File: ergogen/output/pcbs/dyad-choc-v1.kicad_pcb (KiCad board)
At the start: 2 copper layers, 244.9 x 109.6 mm, 78 parts

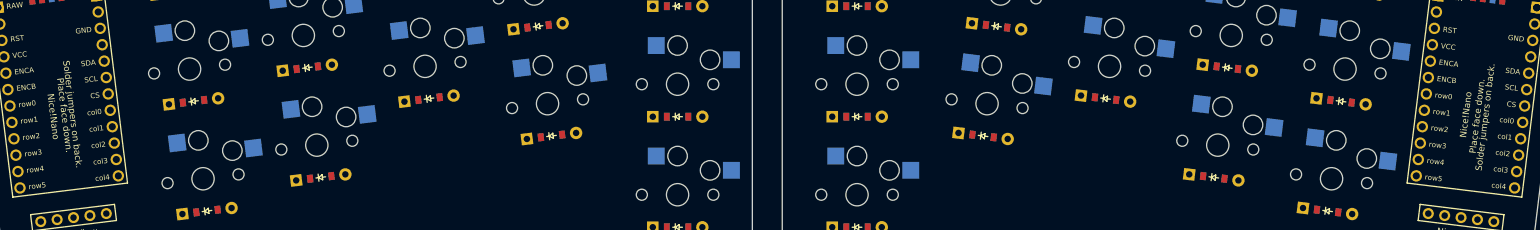
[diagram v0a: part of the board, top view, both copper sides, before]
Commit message: label reformating
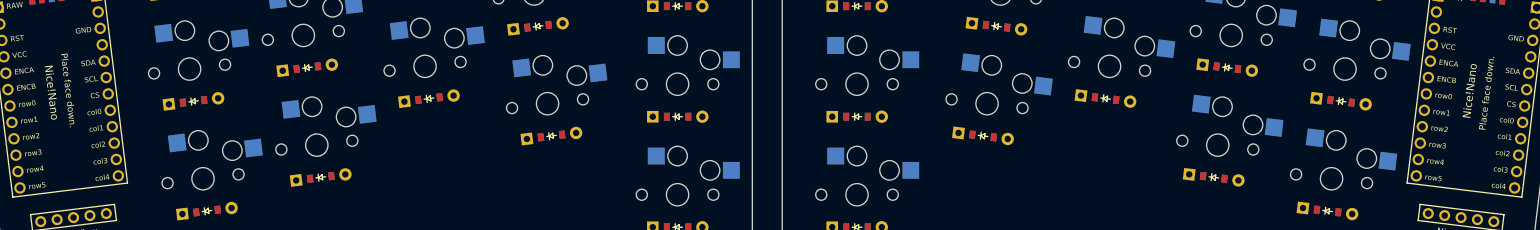
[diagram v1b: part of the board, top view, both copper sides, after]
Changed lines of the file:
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@@
   (page A3)
   (title_block
-    (title Dyad-V1)
+    (title dyad-choc-v1)
     (rev v1.0.0)
     (company Unknown)
@@
           (fp_text user col3 (at 11.43 -6.3 -7) (layer B.SilkS) (effects (font (size 0.8 0.8) (thickness 0.15)) (justify left mirror)))
           (fp_text user col4 (at 13.97 -6.3 -7) (layer B.SilkS) (effects (font (size 0.8 0.8) (thickness 0.15)) (justify left mirror)))
-          (fp_text user "Nice!Nano" (at 3.7 1.2 -97) (layer F.SilkS knockout) (effects (font (size 1.0 1.0) (thickness 0.15))))
-          (fp_text user "Place face down." (at 3.7 -0.55 -97) (layer F.SilkS) (effects (font (size 1.0 1.0) (thickness 0.15))))
-          (fp_text user "Solder jumpers on back." (at 3.7 -1.8 -97) (layer F.SilkS) (effects (font (size 1.0 1.0) (thickness 0.15))))
-          (fp_text user "Nice!Nano" (at 3.7 1.2 -97) (layer B.SilkS knockout) (effects (font (size 1.0 1.0) (thickness 0.15)) (justify mirror)))
-          (fp_text user "Place face down." (at 3.7 -0.55 -97) (layer B.SilkS) (effects (font (size 1.0 1.0) (thickness 0.15)) (justify mirror)))
-          (fp_text user "Solder jumpers on back." (at 3.7 -1.8 -97) (layer B.SilkS) (effects (font (size 1.0 1.0) (thickness 0.15)) (justify mirror)))
+          (fp_text user "Nice!Nano" (at 0 1 -97) (layer F.SilkS knockout) (effects (font (size 1.2 1.2) (thickness 0.30))))
+          (fp_text user "Place face down." (at 0 -1.6 -97) (layer F.SilkS) (effects (font (size 1.0 1.0) (thickness 0.15))))
           (pad 1 thru_hole circle (at -13.97 7.62 -97) (size 1.7526 1.7526) (drill 1.0922) (layers *.Cu *.SilkS *.Mask) (net 35 "RAW"))
           (pad 2 thru_hole circle (at -11.43 7.62 0) (size 1.7526 1.7526) (drill 1.0922) (layers *.Cu *.SilkS *.Mask) (net 36 "GND"))
@@
           (fp_text user col3 (at 11.43 -6.3 7) (layer B.SilkS) (effects (font (size 0.8 0.8) (thickness 0.15)) (justify left mirror)))
           (fp_text user col4 (at 13.97 -6.3 7) (layer B.SilkS) (effects (font (size 0.8 0.8) (thickness 0.15)) (justify left mirror)))
-          (fp_text user "Nice!Nano" (at 3.7 1.2 -83) (layer F.SilkS knockout) (effects (font (size 1.0 1.0) (thickness 0.15))))
-          (fp_text user "Place face down." (at 3.7 -0.55 -83) (layer F.SilkS) (effects (font (size 1.0 1.0) (thickness 0.15))))
-          (fp_text user "Solder jumpers on back." (at 3.7 -1.8 -83) (layer F.SilkS) (effects (font (size 1.0 1.0) (thickness 0.15))))
-          (fp_text user "Nice!Nano" (at 3.7 1.2 -83) (layer B.SilkS knockout) (effects (font (size 1.0 1.0) (thickness 0.15)) (justify mirror)))
-          (fp_text user "Place face down." (at 3.7 -0.55 -83) (layer B.SilkS) (effects (font (size 1.0 1.0) (thickness 0.15)) (justify mirror)))
-          (fp_text user "Solder jumpers on back." (at 3.7 -1.8 -83) (layer B.SilkS) (effects (font (size 1.0 1.0) (thickness 0.15)) (justify mirror)))
+          (fp_text user "Nice!Nano" (at 0 1 -83) (layer F.SilkS knockout) (effects (font (size 1.2 1.2) (thickness 0.30))))
+          (fp_text user "Place face down." (at 0 -1.6 -83) (layer F.SilkS) (effects (font (size 1.0 1.0) (thickness 0.15))))
           (pad 1 thru_hole circle (at -13.97 7.62 -83) (size 1.7526 1.7526) (drill 1.0922) (layers *.Cu *.SilkS *.Mask) (net 35 "RAW"))
           (pad 2 thru_hole circle (at -11.43 7.62 0) (size 1.7526 1.7526) (drill 1.0922) (layers *.Cu *.SilkS *.Mask) (net 36 "GND"))

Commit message: adding text labels
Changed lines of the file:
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@@
           (fp_text user col3 (at 11.43 -6.3 -7) (layer B.SilkS) (effects (font (size 0.8 0.8) (thickness 0.15)) (justify left mirror)))
           (fp_text user col4 (at 13.97 -6.3 -7) (layer B.SilkS) (effects (font (size 0.8 0.8) (thickness 0.15)) (justify left mirror)))
-          (fp_text user "Nice!Nano" (at 0 1 -97) (layer F.SilkS knockout) (effects (font (size 1.2 1.2) (thickness 0.30))))
+          (fp_text user "Nice!Nano" (at 0 1 -97) (layer F.SilkS knockout) (effects (font (size 1.2 1.2) (thickness 0.20))))
           (fp_text user "Place face down." (at 0 -1.6 -97) (layer F.SilkS) (effects (font (size 1.0 1.0) (thickness 0.15))))
           (pad 1 thru_hole circle (at -13.97 7.62 -97) (size 1.7526 1.7526) (drill 1.0922) (layers *.Cu *.SilkS *.Mask) (net 35 "RAW"))
@@
           (fp_text user col3 (at 11.43 -6.3 7) (layer B.SilkS) (effects (font (size 0.8 0.8) (thickness 0.15)) (justify left mirror)))
           (fp_text user col4 (at 13.97 -6.3 7) (layer B.SilkS) (effects (font (size 0.8 0.8) (thickness 0.15)) (justify left mirror)))
-          (fp_text user "Nice!Nano" (at 0 1 -83) (layer F.SilkS knockout) (effects (font (size 1.2 1.2) (thickness 0.30))))
+          (fp_text user "Nice!Nano" (at 0 1 -83) (layer F.SilkS knockout) (effects (font (size 1.2 1.2) (thickness 0.20))))
           (fp_text user "Place face down." (at 0 -1.6 -83) (layer F.SilkS) (effects (font (size 1.0 1.0) (thickness 0.15))))
           (pad 1 thru_hole circle (at -13.97 7.62 -83) (size 1.7526 1.7526) (drill 1.0922) (layers *.Cu *.SilkS *.Mask) (net 35 "RAW"))
@@
                 (pad 2 smd rect (at -0.75 2.075 -7) (size 0.9 1.25) (layers F.Cu F.Paste F.Mask) (net 35 "RAW"))
                 (pad 3 smd rect (at -2.25 2.075 -7) (size 0.9 1.25) (layers F.Cu F.Paste F.Mask))
+                (fp_text user "Power" (at 0 3.6 -7) (layer F.SilkS knockout) (effects (font (size 0.8 0.8) (thickness 0.15))))
                 (fp_line (start 1.95 -1.35) (end -1.95 -1.35) (layer B.SilkS) (width 0.15))
                 (fp_line (start 0 -1.35) (end -3.3 -1.35) (layer B.SilkS) (width 0.15))
@@
                 (pad 2 smd rect (at 0.75 2.075 -7) (size 0.9 1.25) (layers B.Cu B.Paste B.Mask) (net 35 "RAW"))
                 (pad 3 smd rect (at 2.25 2.075 -7) (size 0.9 1.25) (layers B.Cu B.Paste B.Mask))
+                (fp_text user "Power" (at 0 3.6 -7) (layer F.SilkS knockout) (effects (font (size 0.8 0.8) (thickness 0.15))))
                 )
             (module E73:SPDT_C128955 (layer F.Cu)
@@
                 (pad 2 smd rect (at -0.75 2.075 7) (size 0.9 1.25) (layers F.Cu F.Paste F.Mask) (net 35 "RAW"))
                 (pad 3 smd rect (at -2.25 2.075 7) (size 0.9 1.25) (layers F.Cu F.Paste F.Mask))
+                (fp_text user "Power" (at 0 3.6 7) (layer F.SilkS knockout) (effects (font (size 0.8 0.8) (thickness 0.15))))
                 (fp_line (start 1.95 -1.35) (end -1.95 -1.35) (layer B.SilkS) (width 0.15))
                 (fp_line (start 0 -1.35) (end -3.3 -1.35) (layer B.SilkS) (width 0.15))
@@
                 (pad 2 smd rect (at 0.75 2.075 7) (size 0.9 1.25) (layers B.Cu B.Paste B.Mask) (net 35 "RAW"))
                 (pad 3 smd rect (at 2.25 2.075 7) (size 0.9 1.25) (layers B.Cu B.Paste B.Mask))
+                (fp_text user "Power" (at 0 3.6 7) (layer F.SilkS knockout) (effects (font (size 0.8 0.8) (thickness 0.15))))
                 )
             (module lib:niceview_headers (layer F.Cu)
@@
       (pad "1" thru_hole circle (at -3.2 0 173) (size 2 2) (drill 1) (layers "*.Cu" "*.Mask") (net 36 "GND"))
       (pad "2" thru_hole circle (at 3.2 0 173) (size 2 2) (drill 1) (layers "*.Cu" "*.Mask") (net 37 "RST"))
+      (fp_text user "Reset" (at 0 -3 173) (layer F.SilkS knockout) (effects (font (size 0.8 0.8) (thickness 0.15))))
     )
     (module PTS636_SP43_LFS (layer F.Cu)
@@
       (pad "1" thru_hole circle (at -3.2 0 -173) (size 2 2) (drill 1) (layers "*.Cu" "*.Mask") (net 36 "GND"))
       (pad "2" thru_hole circle (at 3.2 0 -173) (size 2 2) (drill 1) (layers "*.Cu" "*.Mask") (net 37 "RST"))
+      (fp_text user "Reset" (at 0 -3 -173) (layer F.SilkS knockout) (effects (font (size 0.8 0.8) (thickness 0.15))))
     )
             (gr_line (start 220.5 171) (end 241.15492522211616 171) (angle 90) (layer Edge.Cuts) (width 0.15))

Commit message: iterating routes
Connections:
- net inner_default renamed inner_sole
- net mirror_inner_default renamed mirror_inner_sole
- net mirror_outer_default renamed mirror_outer_sole
- net mirror_pinkey_height_bottom renamed mirror_pinky_bottom
- net mirror_pinkey_height_home renamed mirror_pinky_home
- net mirror_pinkey_height_top renamed mirror_pinky_top
- net outer_default renamed outer_sole
- net pinkey_height_bottom renamed pinky_bottom
- net pinkey_height_home renamed pinky_home
- net pinkey_height_top renamed pinky_top
- D1 pad 1: (no net) -> P8
- D10 pad 1: (no net) -> P8
- D11 pad 1: (no net) -> P7
- D12 pad 1: (no net) -> P6
- D13 pad 1: (no net) -> P8
- D14 pad 1: (no net) -> P7
- D15 pad 1: (no net) -> P6
- D16 pad 1: (no net) -> P9
- D17 pad 1: (no net) -> P9
- D18 pad 1: (no net) -> P8
- D19 pad 1: (no net) -> P7
- D2 pad 1: (no net) -> P7
- D20 pad 1: (no net) -> P6
- D21 pad 1: (no net) -> P8
- D22 pad 1: (no net) -> P7
- D23 pad 1: (no net) -> P6
- D24 pad 1: (no net) -> P8
- D25 pad 1: (no net) -> P7
- D26 pad 1: (no net) -> P6
- D27 pad 1: (no net) -> P8
- D28 pad 1: (no net) -> P7
- D29 pad 1: (no net) -> P6
- D3 pad 1: (no net) -> P6
- D30 pad 1: (no net) -> P8
- D31 pad 1: (no net) -> P7
- D32 pad 1: (no net) -> P6
- D33 pad 1: (no net) -> P9
- D34 pad 1: (no net) -> P9
- D4 pad 1: (no net) -> P8
- D5 pad 1: (no net) -> P7
- D6 pad 1: (no net) -> P6
- D7 pad 1: (no net) -> P8
- D8 pad 1: (no net) -> P7
- D9 pad 1: (no net) -> P6
- MCU1 pad : P1 -> CS
- MCU1 pad 13: P1 -> CS
- MCU1 pad 17: P2 -> MOSI
- MCU1 pad 18: P3 -> SCK
- MCU2 pad : P1 -> CS
- MCU2 pad 13: P1 -> CS
- MCU2 pad 17: P2 -> MOSI
- MCU2 pad 18: P3 -> SCK
- Nice!View1 pad 1: NN_CS_SDA -> CS
- Nice!View1 pad 2: NN_VCC -> VCC
- Nice!View1 pad 3: NN_SCL_GND -> SCK
- Nice!View1 pad 4: NN_SDA_CS -> MOSI
- Nice!View2 pad 1: NN_CS_SDA -> CS
- Nice!View2 pad 2: NN_VCC -> VCC
- Nice!View2 pad 3: NN_SCL_GND -> SCK
- Nice!View2 pad 4: NN_SDA_CS -> MOSI
- S1 pad 1: (no net) -> P18
- S10 pad 1: (no net) -> P16
- S11 pad 1: (no net) -> P16
- S12 pad 1: (no net) -> P16
- S13 pad 1: (no net) -> P10
- S14 pad 1: (no net) -> P10
- S15 pad 1: (no net) -> P10
- S16 pad 1: (no net) -> P16
- S17 pad 1: (no net) -> P10
- S18 pad 1: (no net) -> P18
- S19 pad 1: (no net) -> P18
- S2 pad 1: (no net) -> P18
- S20 pad 1: (no net) -> P18
- S21 pad 1: (no net) -> P15
- S22 pad 1: (no net) -> P15
- S23 pad 1: (no net) -> P15
- S24 pad 1: (no net) -> P14
- S25 pad 1: (no net) -> P14
- S26 pad 1: (no net) -> P14
- S27 pad 1: (no net) -> P16
- S28 pad 1: (no net) -> P16
- S29 pad 1: (no net) -> P16
- S3 pad 1: (no net) -> P18
- S30 pad 1: (no net) -> P10
- S31 pad 1: (no net) -> P10
- S32 pad 1: (no net) -> P10
- S33 pad 1: (no net) -> P16
- S34 pad 1: (no net) -> P10
- S4 pad 1: (no net) -> P15
- S5 pad 1: (no net) -> P15
- S6 pad 1: (no net) -> P15
- S7 pad 1: (no net) -> P14
- S8 pad 1: (no net) -> P14
- S9 pad 1: (no net) -> P14

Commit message: completing routes
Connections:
- ? pad 1: RAW -> POSITIVE (x2)
- T1 pad 1: switch_from -> POSITIVE
- T2 pad 1: switch_from -> POSITIVE
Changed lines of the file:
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@@
 (net 55 "P4")
 (net 56 "P5")
-(net 57 "switch_from")
+(net 57 "POSITIVE")
   (net_class Default "This is the default net class."
     (clearance 0.2)
@@
 (add_net "P4")
 (add_net "P5")
-(add_net "switch_from")
+(add_net "POSITIVE")
   )
       (module PG1350 (layer F.Cu)
@@
         (fp_text user + (at 0 6.3 173) (layer B.SilkS) (effects (font (size 0.8 0.8) (thickness 0.15))))
         (fp_text user - (at 0 -6.3 173) (layer B.SilkS) (effects (font (size 0.8 0.8) (thickness 0.15))))
-        (pad 1 thru_hole rect (at 0 7.75 83) (size 1.4 1.4) (drill 0.8) (layers *.Cu *.SilkS *.Mask) (net 44 "RAW"))
+        (pad 1 thru_hole rect (at 0 7.75 83) (size 1.4 1.4) (drill 0.8) (layers *.Cu *.SilkS *.Mask) (net 57 "POSITIVE"))
         (pad 2 thru_hole circle (at 0 -7.75 83) (size 1.4 1.4) (drill 0.8) (layers *.Cu *.SilkS *.Mask) (net 45 "GND"))
         )
@@
         (fp_text user + (at 0 6.3 7) (layer B.SilkS) (effects (font (size 0.8 0.8) (thickness 0.15))))
         (fp_text user - (at 0 -6.3 7) (layer B.SilkS) (effects (font (size 0.8 0.8) (thickness 0.15))))
-        (pad 1 thru_hole rect (at 0 7.75 -83) (size 1.4 1.4) (drill 0.8) (layers *.Cu *.SilkS *.Mask) (net 44 "RAW"))
+        (pad 1 thru_hole rect (at 0 7.75 -83) (size 1.4 1.4) (drill 0.8) (layers *.Cu *.SilkS *.Mask) (net 57 "POSITIVE"))
         (pad 2 thru_hole circle (at 0 -7.75 -83) (size 1.4 1.4) (drill 0.8) (layers *.Cu *.SilkS *.Mask) (net 45 "GND"))
         )
@@
                 (pad "" smd rect (at -3.7 1.1 -7) (size 0.9 0.9) (layers B.Cu B.Paste B.Mask))
                 (pad "" smd rect (at -3.7 -1.1 -7) (size 0.9 0.9) (layers B.Cu B.Paste B.Mask))
-                (pad 1 smd rect (at -2.25 2.075 -7) (size 0.9 1.25) (layers B.Cu B.Paste B.Mask) (net 57 "switch_from"))
+                (pad 1 smd rect (at -2.25 2.075 -7) (size 0.9 1.25) (layers B.Cu B.Paste B.Mask) (net 57 "POSITIVE"))
                 (pad 2 smd rect (at 0.75 2.075 -7) (size 0.9 1.25) (layers B.Cu B.Paste B.Mask) (net 44 "RAW"))
                 (pad 3 smd rect (at 2.25 2.075 -7) (size 0.9 1.25) (layers B.Cu B.Paste B.Mask))
-                (fp_text user "Power" (at 0 3.6 -7) (layer F.SilkS knockout) (effects (font (size 0.8 0.8) (thickness 0.15))))
-                (fp_line (start 1.95 -1.35) (end -1.95 -1.35) (layer F.SilkS) (width 0.15))
-                (fp_line (start 0 -1.35) (end -3.3 -1.35) (layer F.SilkS) (width 0.15))
-                (fp_line (start -3.3 -1.35) (end -3.3 1.5) (layer F.SilkS) (width 0.15))
-                (fp_line (start -3.3 1.5) (end 3.3 1.5) (layer F.SilkS) (width 0.15))
-                (fp_line (start 3.3 1.5) (end 3.3 -1.35) (layer F.SilkS) (width 0.15))
-                (fp_line (start 0 -1.35) (end 3.3 -1.35) (layer F.SilkS) (width 0.15))
-                (pad "" smd rect (at 3.7 -1.1 -7) (size 0.9 0.9) (layers F.Cu F.Paste F.Mask))
-                (pad "" smd rect (at 3.7 1.1 -7) (size 0.9 0.9) (layers F.Cu F.Paste F.Mask))
-                (pad "" smd rect (at -3.7 1.1 -7) (size 0.9 0.9) (layers F.Cu F.Paste F.Mask))
-                (pad "" smd rect (at -3.7 -1.1 -7) (size 0.9 0.9) (layers F.Cu F.Paste F.Mask))
-                (pad 1 smd rect (at 2.25 2.075 -7) (size 0.9 1.25) (layers F.Cu F.Paste F.Mask) (net 57 "switch_from"))
-                (pad 2 smd rect (at -0.75 2.075 -7) (size 0.9 1.25) (layers F.Cu F.Paste F.Mask) (net 44 "RAW"))
-                (pad 3 smd rect (at -2.25 2.075 -7) (size 0.9 1.25) (layers F.Cu F.Paste F.Mask))
                 (fp_text user "Power" (at 0 3.6 -7) (layer F.SilkS knockout) (effects (font (size 0.8 0.8) (thickness 0.15))))
                 )
@@
                 (pad "" smd rect (at -3.7 1.1 7) (size 0.9 0.9) (layers B.Cu B.Paste B.Mask))
                 (pad "" smd rect (at -3.7 -1.1 7) (size 0.9 0.9) (layers B.Cu B.Paste B.Mask))
-                (pad 1 smd rect (at -2.25 2.075 7) (size 0.9 1.25) (layers B.Cu B.Paste B.Mask) (net 57 "switch_from"))
+                (pad 1 smd rect (at -2.25 2.075 7) (size 0.9 1.25) (layers B.Cu B.Paste B.Mask) (net 57 "POSITIVE"))
                 (pad 2 smd rect (at 0.75 2.075 7) (size 0.9 1.25) (layers B.Cu B.Paste B.Mask) (net 44 "RAW"))
                 (pad 3 smd rect (at 2.25 2.075 7) (size 0.9 1.25) (layers B.Cu B.Paste B.Mask))
                 (fp_text user "Power" (at 0 3.6 7) (layer F.SilkS knockout) (effects (font (size 0.8 0.8) (thickness 0.15))))
-                (fp_line (start 1.95 -1.35) (end -1.95 -1.35) (layer F.SilkS) (width 0.15))
-                (fp_line (start 0 -1.35) (end -3.3 -1.35) (layer F.SilkS) (width 0.15))
-                (fp_line (start -3.3 -1.35) (end -3.3 1.5) (layer F.SilkS) (width 0.15))
-                (fp_line (start -3.3 1.5) (end 3.3 1.5) (layer F.SilkS) (width 0.15))
-                (fp_line (start 3.3 1.5) (end 3.3 -1.35) (layer F.SilkS) (width 0.15))
-                (fp_line (start 0 -1.35) (end 3.3 -1.35) (layer F.SilkS) (width 0.15))
-                (pad "" smd rect (at 3.7 -1.1 7) (size 0.9 0.9) (layers F.Cu F.Paste F.Mask))
-                (pad "" smd rect (at 3.7 1.1 7) (size 0.9 0.9) (layers F.Cu F.Paste F.Mask))
-                (pad "" smd rect (at -3.7 1.1 7) (size 0.9 0.9) (layers F.Cu F.Paste F.Mask))
-                (pad "" smd rect (at -3.7 -1.1 7) (size 0.9 0.9) (layers F.Cu F.Paste F.Mask))
-                (pad 1 smd rect (at 2.25 2.075 7) (size 0.9 1.25) (layers F.Cu F.Paste F.Mask) (net 57 "switch_from"))
-                (pad 2 smd rect (at -0.75 2.075 7) (size 0.9 1.25) (layers F.Cu F.Paste F.Mask) (net 44 "RAW"))
-                (pad 3 smd rect (at -2.25 2.075 7) (size 0.9 1.25) (layers F.Cu F.Paste F.Mask))
-                (fp_text user "Power" (at 0 3.6 7) (layer F.SilkS knockout) (effects (font (size 0.8 0.8) (thickness 0.15))))
                 )

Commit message: continuing to refine
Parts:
- removed the ? at (321.7, 173.4)
- removed the ? at (110.7, 173.4)
- added ?: , Button_Switch_SMD:SW_SPST_B3U-1000P, F.Cu at (321.7, 173.4)
- added ?: , Button_Switch_SMD:SW_SPST_B3U-1000P, F.Cu at (114.3, 173.4)
- moved ? 3.60 mm to (108.7, 127.8), turned to 97 degrees
- moved D18 3.60 mm to (206.0, 165.0)
- moved D19 3.60 mm to (206.0, 148.0)
- moved D20 3.60 mm to (206.0, 131.0)
- moved D21 3.60 mm to (186.6, 151.0)
- moved D22 3.60 mm to (184.5, 134.1)
- moved D23 3.60 mm to (182.5, 117.2)
- moved D24 3.60 mm to (167.8, 145.2)
- moved D25 3.60 mm to (165.7, 128.3)
- moved D26 3.60 mm to (163.6, 111.5)
- moved D27 3.60 mm to (151.1, 157.3)
- moved D28 3.60 mm to (149.0, 140.5)
- moved D29 3.60 mm to (147.0, 123.6)
- moved D30 3.60 mm to (133.6, 162.5)
- moved D31 3.60 mm to (131.5, 145.6)
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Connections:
- T1 pad 1: POSITIVE -> RAW
- T1 pad 2: RAW -> POSITIVE
- T2 pad 1: POSITIVE -> RAW
- T2 pad 2: RAW -> POSTIVE
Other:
- board size 244.9 x 109.6 mm -> 238.4 x 105.9 mm

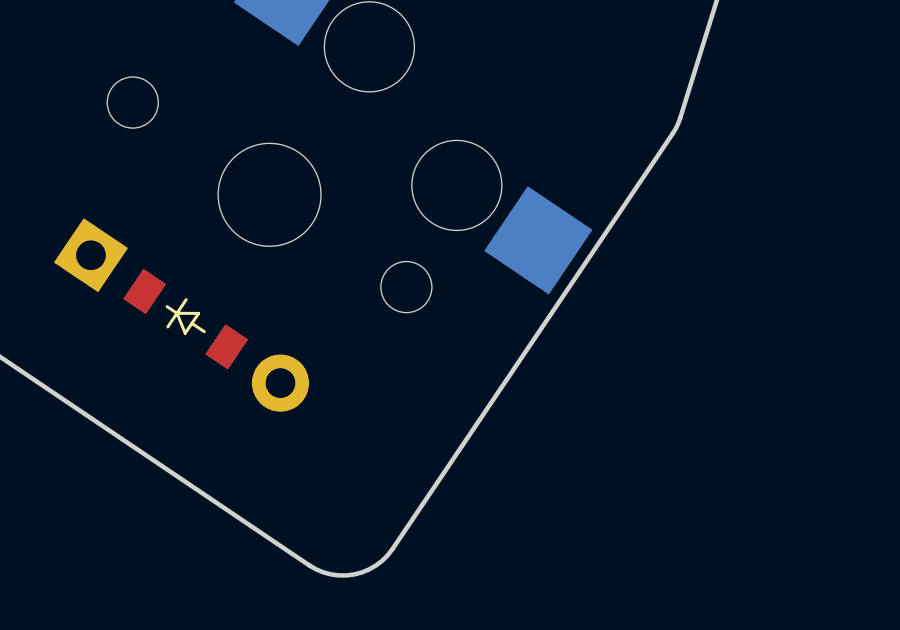
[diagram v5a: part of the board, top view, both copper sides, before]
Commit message: adding via example
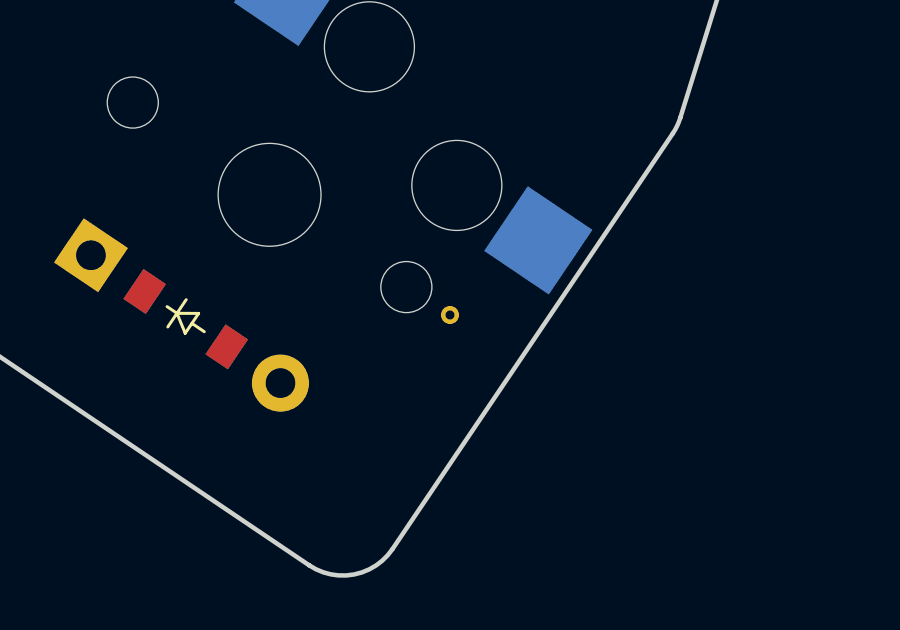
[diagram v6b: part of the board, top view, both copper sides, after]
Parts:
- added REF**: VIA-0.6mm, VIA-0.6mm, F.Cu at (319.3, 193.3)
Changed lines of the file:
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@@
 	  (pad 2 smd rect (at 1.7 0 187) (size 0.9 1.7) (layers F.Cu F.Paste F.Mask) (net 45 "GND"))
 		  )
+      (module VIA-0.6mm (layer F.Cu)
+      (at 319.2527186 193.29229289999998 -7)
+      (fp_text reference REF** (at 0 1.4) (layer F.SilkS) hide (effects (font (size 1 1) (thickness 0.15))))
+      (fp_text value VIA-0.6mm (at 0 -1.4) (layer F.Fab) hide (effects (font (size 1 1) (thickness 0.15))))
+      (pad 1 thru_hole circle (at 0 0) (size 0.6 0.6) (drill 0.3) (layers *.Cu) (zone_connect 2) (net 44 "RAW"))
+      )
             (gr_line (start 222 169.5) (end 239.6672239474708 169.5) (angle 90) (layer Edge.Cuts) (width 0.15))
 (gr_line (start 220 167.5) (end 220 118.5) (angle 90) (layer Edge.Cuts) (width 0.15))
